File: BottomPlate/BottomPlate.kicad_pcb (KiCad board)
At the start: 2 copper layers, 135.3 x 94.8 mm, 5 parts

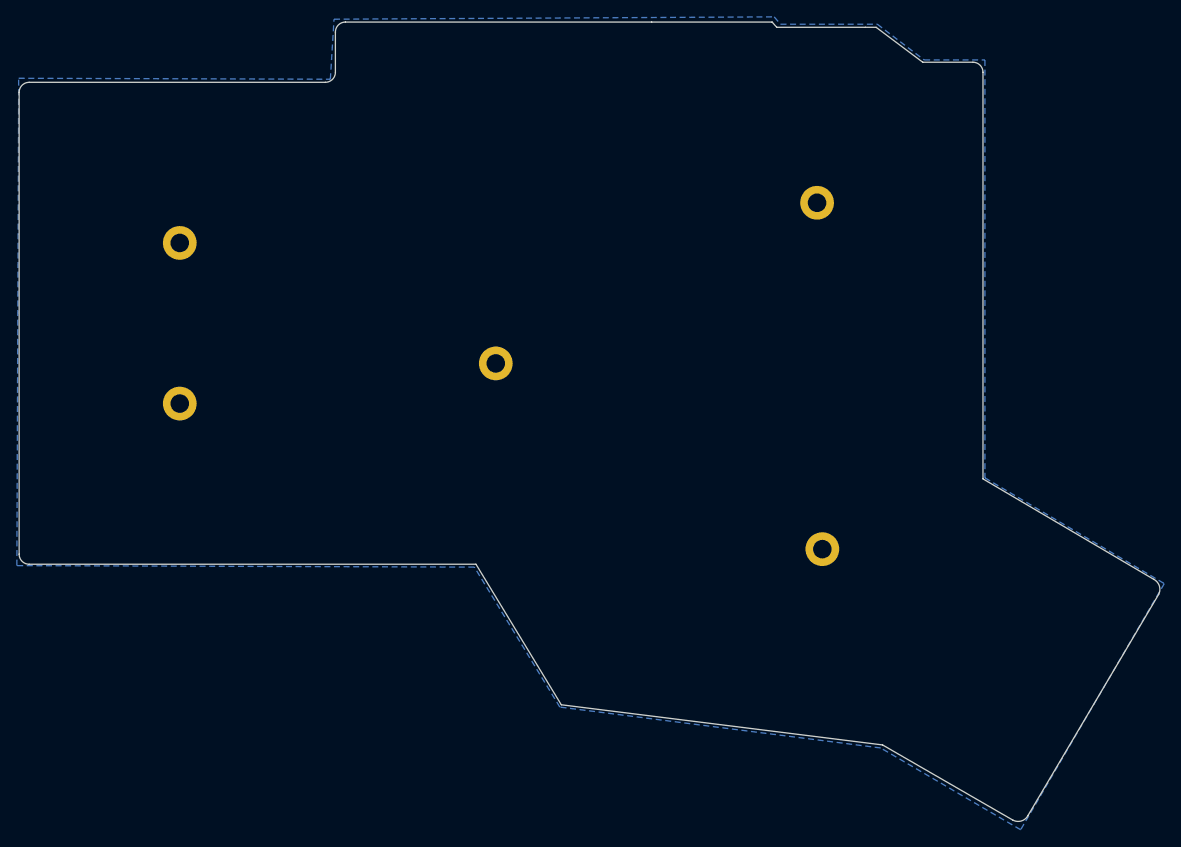
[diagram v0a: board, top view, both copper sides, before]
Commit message: Add front copper layer
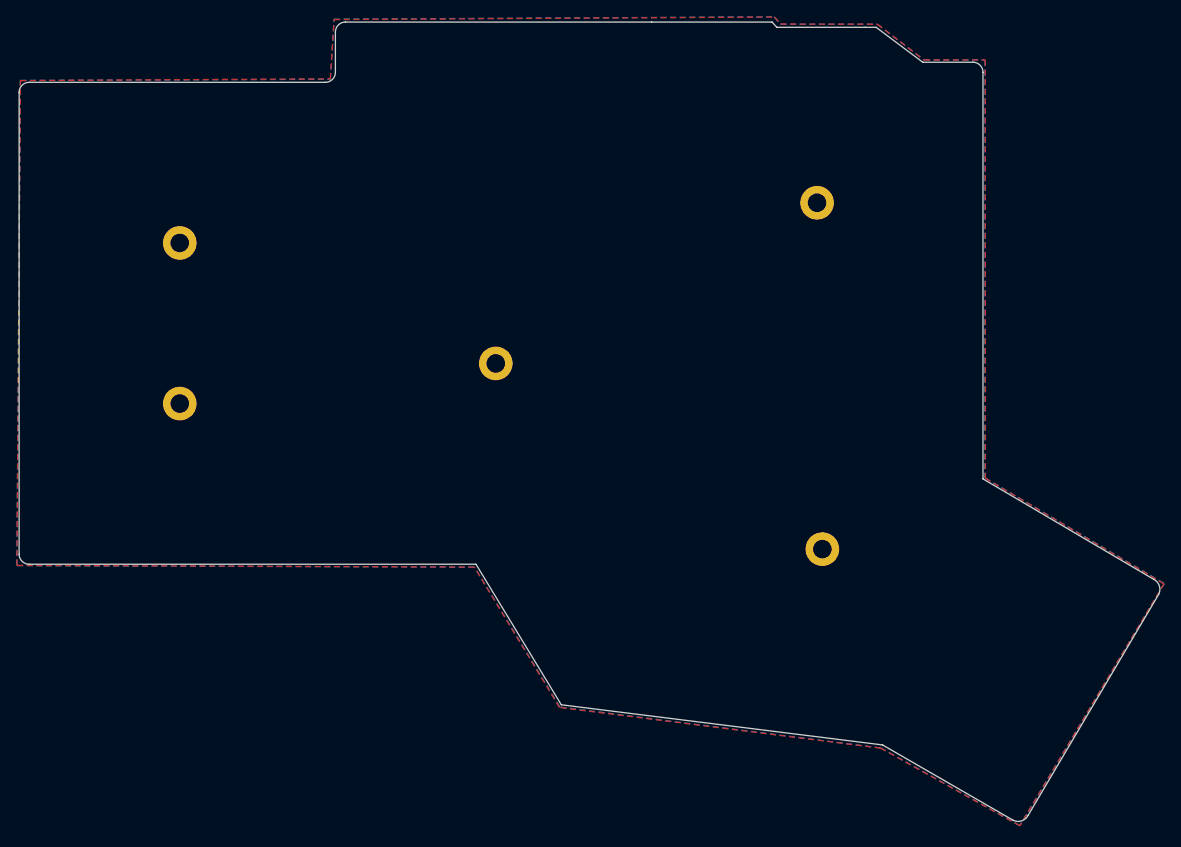
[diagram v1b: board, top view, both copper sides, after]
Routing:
- added copper zone on F.Cu, net (none)
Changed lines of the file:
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@@
       (pts
         (xy 176.60366 50.9143) (xy 188.09208 50.9143) (xy 193.63944 55.15102) (xy 200.84796 55.15102) (xy 200.84796 104.7115)
-        (xy 222.12046 117.2464) (xy 205.08468 146.43862) (xy 188.48578 136.7409) (xy 150.43658 131.89204) (xy 140.30198 115.29314)
-        (xy 86.04758 115.11788) (xy 86.26602 57.32272) (xy 123.22302 57.43702) (xy 123.6599 50.3174) (xy 175.85944 50.04054)
+        (xy 222.12046 117.2464) (xy 204.98308 145.95856) (xy 188.48578 136.7409) (xy 150.43658 131.89204) (xy 140.30198 115.29314)
+        (xy 86.04758 115.11788) (xy 86.45906 57.58688) (xy 123.22302 57.43702) (xy 123.6599 50.3174) (xy 175.85944 50.04054)
       )
     )
+  )
+  (zone (net 0) (net_name "") (layer F.Cu) (hatch edge 0.508)
+    (connect_pads (clearance 0.508))
+    (min_thickness 0.254)
+    (fill yes (arc_segments 32) (thermal_gap 0.508) (thermal_bridge_width 0.508))
+    (polygon
+      (pts
+        (xy 176.61636 50.89144) (xy 188.0997 50.91684) (xy 193.62166 55.15864) (xy 200.89114 55.14594) (xy 200.90892 104.75976)
+        (xy 222.07728 117.27434) (xy 204.99578 145.96364) (xy 188.49086 136.76122) (xy 150.40356 131.9403) (xy 140.30198 115.28806)
+        (xy 86.0552 115.08232) (xy 86.46922 57.5945) (xy 123.21794 57.3913) (xy 123.68022 50.36312) (xy 175.88992 50.05832)
+      )
+    )

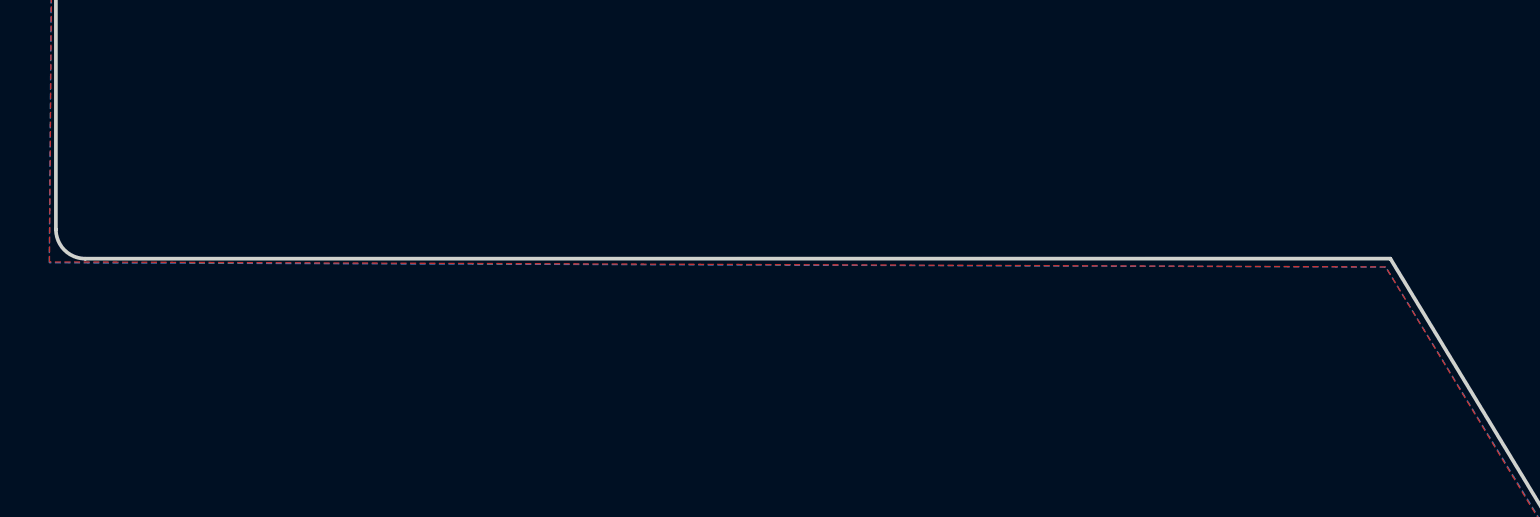
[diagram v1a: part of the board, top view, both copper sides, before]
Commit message: Fix top/bottom plates edges
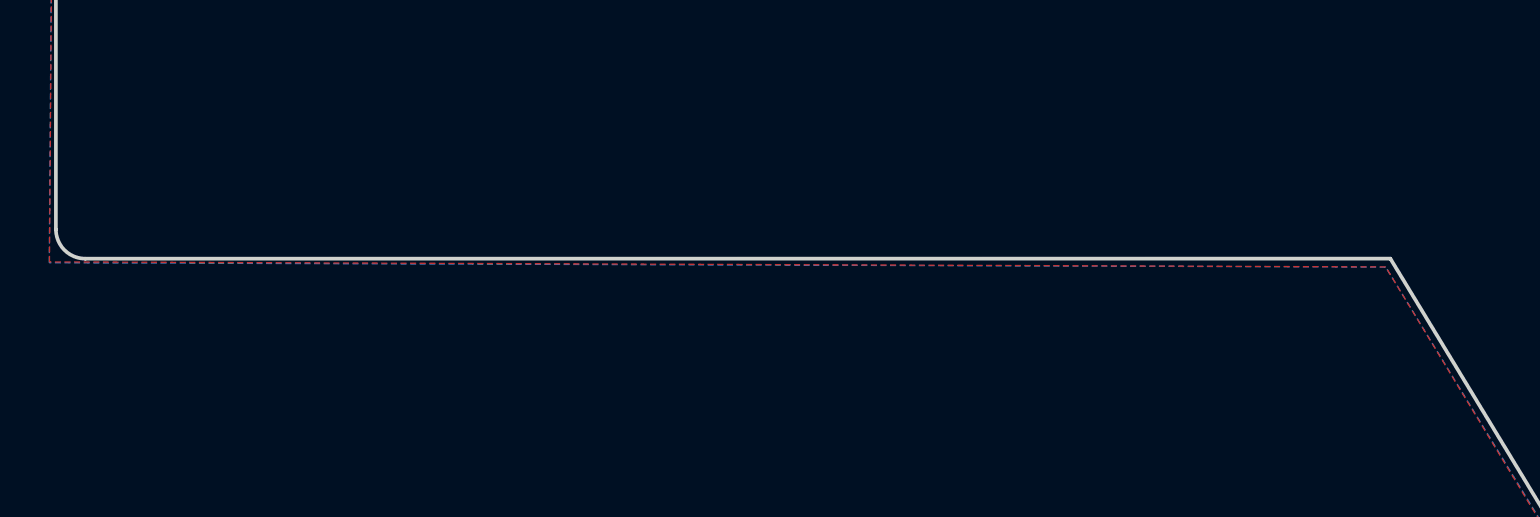
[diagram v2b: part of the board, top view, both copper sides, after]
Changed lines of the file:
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@@
   (gr_line (start 150.61146 131.61897) (end 140.491148 114.95022) (angle 90) (layer Edge.Cuts) (width 0.15))
   (gr_line (start 150.61146 131.61897) (end 188.71146 136.38147) (angle 90) (layer Edge.Cuts) (width 0.15))
-  (gr_line (start 87.50396 114.95272) (end 140.491148 114.95022) (angle 90) (layer Edge.Cuts) (width 0.15))
+  (gr_line (start 87.507085 114.95272) (end 140.491148 114.95022) (angle 90) (layer Edge.Cuts) (width 0.15))
   (gr_line (start 200.61771 56.609595) (end 200.61771 104.829908) (angle 90) (layer Edge.Cuts) (width 0.15))
   (gr_line (start 193.47396 55.41897) (end 199.427085 55.41897) (angle 90) (layer Edge.Cuts) (width 0.15))
